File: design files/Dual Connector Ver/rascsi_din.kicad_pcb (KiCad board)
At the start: 2 copper layers, 67.5 x 66.5 mm, 24 parts, among them J1 Raspberry_Pi_2_3, J2 DB25_Female, J3 Conn_02x25_Odd_Even, U1 SN74LS641-1C, U2 SN74LS641-1C, U3 SN74LS641-1C, U4 SN74LS641-1C

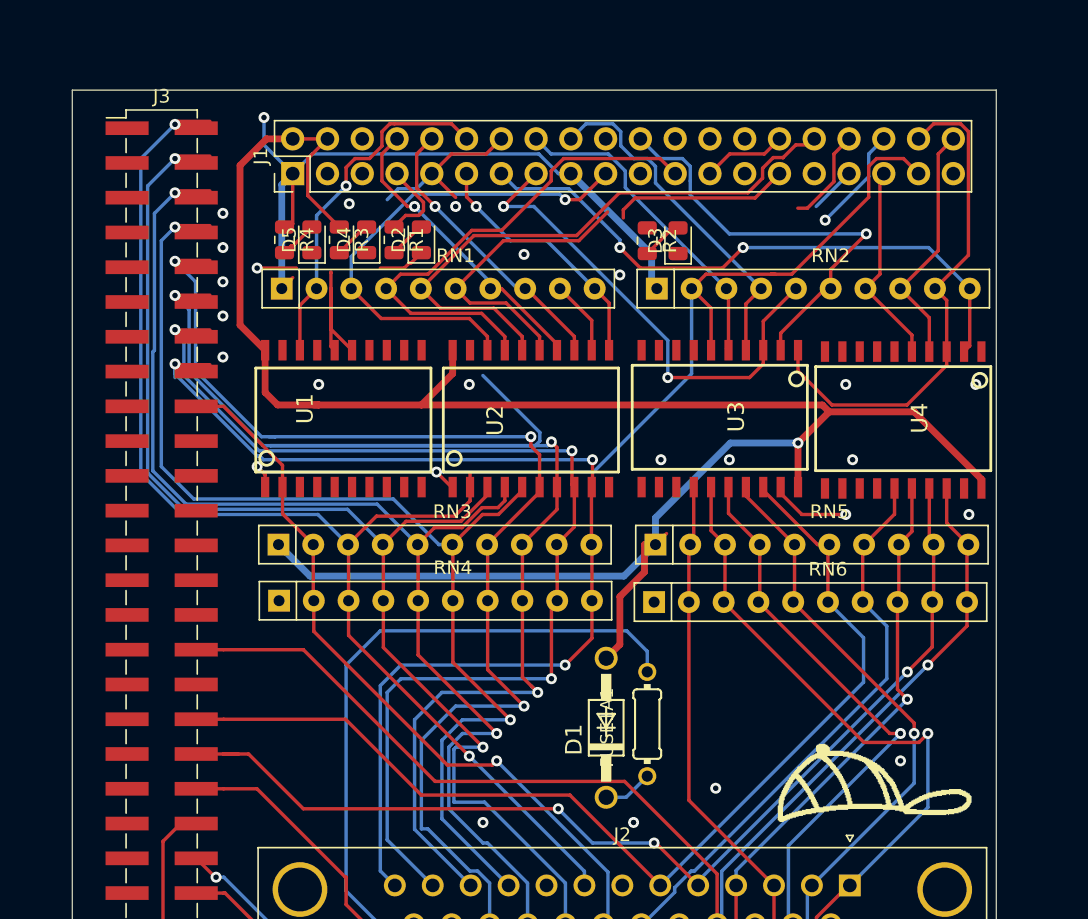
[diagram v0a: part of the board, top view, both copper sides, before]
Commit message: Add silk screen art and clean up labels
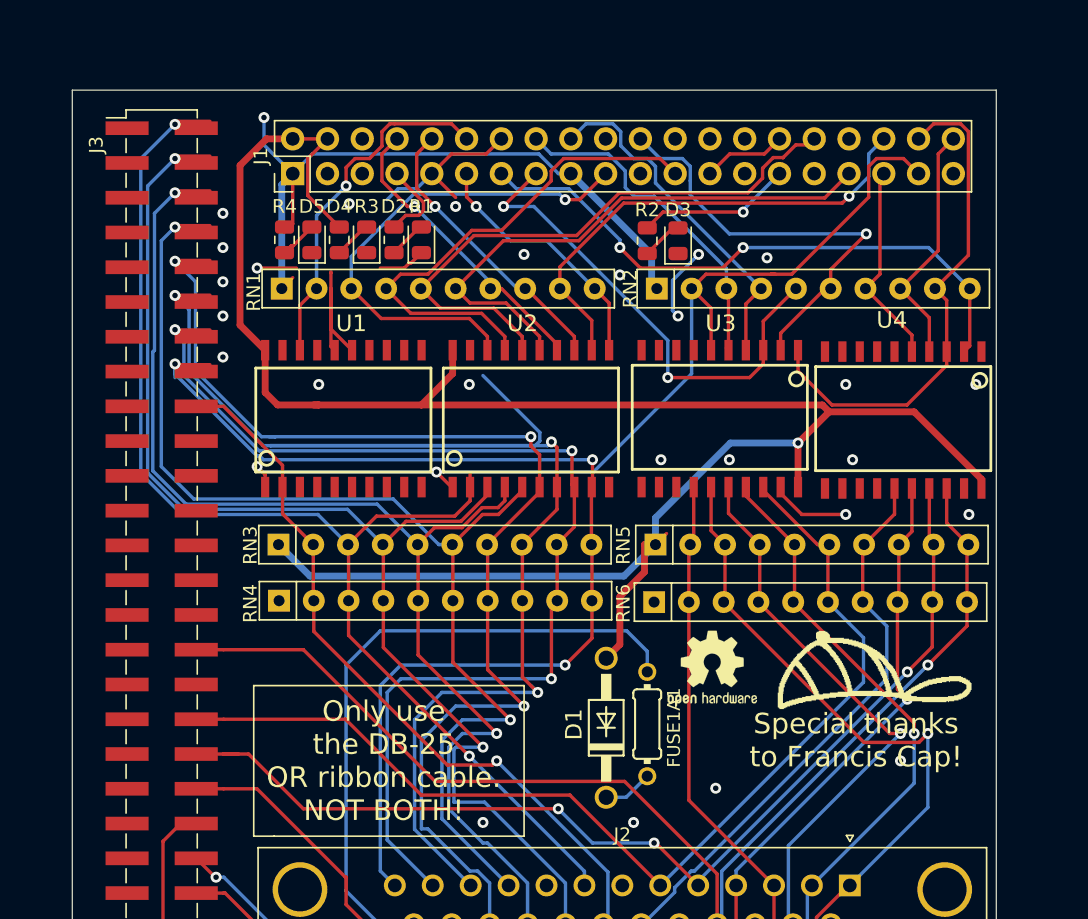
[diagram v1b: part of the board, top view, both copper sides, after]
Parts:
- added REF**: OSHW-Logo2_7.3x6mm_SilkScreen, Symbol:OSHW-Logo2_7.3x6mm_SilkScreen, F.Cu at (100.8, 90.2)
- moved U$1 8.25 mm to (105.5, 93.2)
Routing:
- net PI-D6: track 13.2 -> 35.6 mm
- net PI-D3: track 25.4 -> 40.8 mm
- net DBG_LED: track 13.1 -> 11.2 mm, vias 0 -> 1
- net GND: track 51.5 -> 50.5 mm, vias 24 -> 27
- net PI-REQ: track 23.9 -> 24.8 mm
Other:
- board text added: "Only use the DB-25 OR ribbon cable. NOT BOTH!"
- board text added: "Special thanks to Francis Cap!"

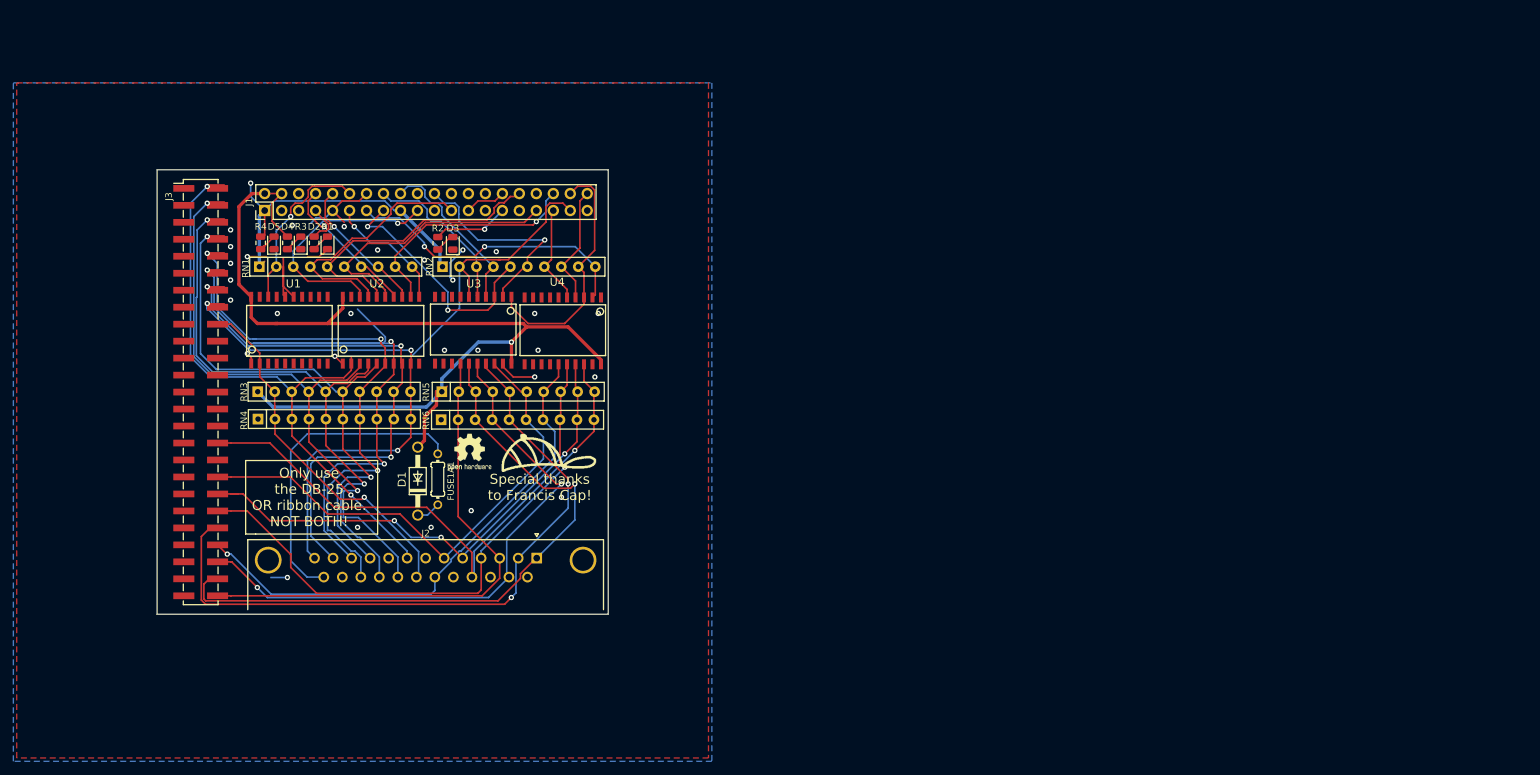
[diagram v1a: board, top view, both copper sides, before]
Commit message: Corrected pinout to match original RaSCSI design.
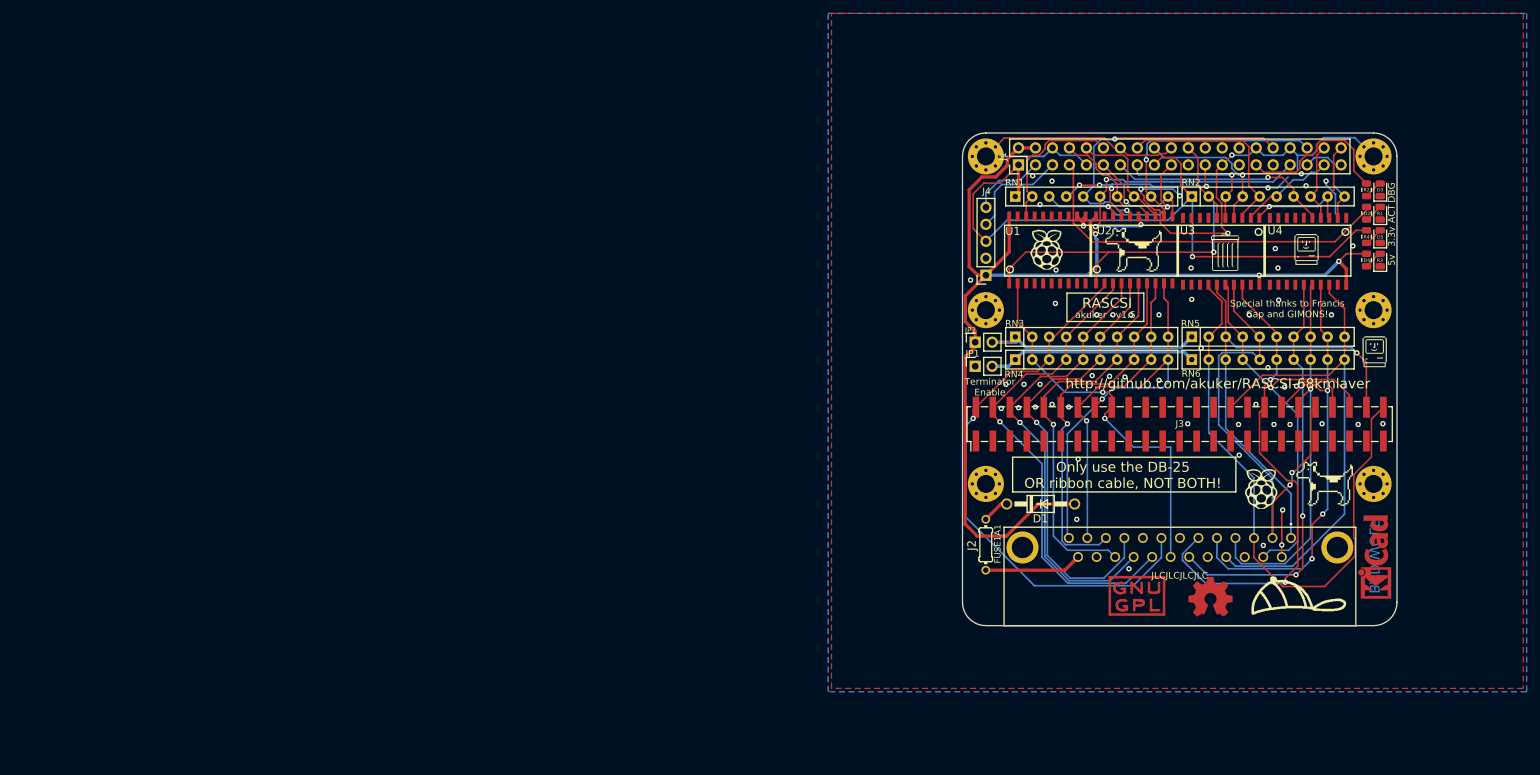
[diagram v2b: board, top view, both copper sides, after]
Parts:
- removed the REF** at (100.8, 90.2)
- added H1: Hole1, MountingHole:MountingHole_2.7mm_M2.5_Pad_Via, F.Cu at (178.0, 46.0)
- added H2: Hole2, MountingHole:MountingHole_2.7mm_M2.5_Pad_Via, F.Cu at (236.0, 46.0)
- added H3: Hole3, MountingHole:MountingHole_2.7mm_M2.5_Pad_Via, F.Cu at (178.0, 69.0)
- added H4: Hole5, MountingHole:MountingHole_2.7mm_M2.5_Pad_Via, F.Cu at (236.0, 69.0)
- added H5: Hole4, MountingHole:MountingHole_2.7mm_M2.5_Pad_Via, F.Cu at (178.0, 95.0)
- added H6: Hole6, MountingHole:MountingHole_2.7mm_M2.5_Pad_Via, F.Cu at (236.0, 95.0)
- added J4: I2C Pinout, Connector_PinSocket_2.54mm:PinSocket_1x05_P2.54mm_Vertical, F.Cu at (178.0, 63.8)
- added JP1: Term_Enable_GND, Connector_PinSocket_2.54mm:PinSocket_1x02_P2.54mm_Vertical, F.Cu at (176.4, 77.4)
- added JP2: Term_Enable_5v, Connector_PinSocket_2.54mm:PinSocket_1x02_P2.54mm_Vertical, F.Cu at (176.4, 73.8)
- added L1: Mac, rascsi_din:mac_happy_small, F.Cu at (226.0, 59.9)
- added L2: Dogcow, rascsi_din:dogcow, F.Cu at (228.7, 95.0)
- added L3: Mac2, rascsi_din:mac_happy_small, F.Cu at (236.2, 75.2)
- added L4: Dogcow2, rascsi_din:dogcow, F.Cu at (200.1, 60.0)
- added L5: Raspberry Pi, rascsi_din:pi_logo, F.Cu at (219.2, 95.8)
- added L6: Mac Trashcan, rascsi_din:mac_trashcan, F.Cu at (213.8, 60.5)
- added L7: Raspberry Pi, rascsi_din:pi_logo, F.Cu at (187.1, 60.0)
- added REF**: KiCad-Logo_5mm_Copper, Symbol:KiCad-Logo_5mm_Copper, F.Cu at (236.7, 105.9)
- added REF**: OSHW-Symbol_6.7x6mm_Copper, Symbol:OSHW-Symbol_6.7x6mm_Copper, F.Cu at (211.6, 111.9)
- added REF**: Symbol_GNU-GPL_CopperTop_Small, Symbol:Symbol_GNU-GPL_CopperTop_Small, F.Cu at (200.6, 112.0)
- J2: value DB25_Female -> DLS3XS6AK44X; footprint Connector_Dsub:DSUB-25_Female_Horizontal_P2.77x2.84mm_EdgePinOffset4.94mm_Housed_MountingHolesOffset7.48mm -> Library_Loader:DLS3XS6AK44X
- R1, R2, R4: value 10k -> 44
- R3: value 10k -> 112
- moved D5 165.5 mm to (237.0, 58.0)
- moved R4 165.5 mm to (234.9, 58.0)
- moved D4 161.5 mm to (237.0, 61.5)
- moved R3 161.5 mm to (234.9, 61.5)
- moved D2 157.6 mm to (237.0, 54.5)
- moved R1 157.5 mm to (234.9, 54.5)
- moved J3 146.5 mm to (207.0, 86.1), turned to 90 degrees
- moved R2 139.2 mm to (234.9, 51.0)
- moved D3 139.0 mm to (237.0, 51.0)
- moved U$1 114.2 mm to (217.7, 114.6)
- moved U1 114.0 mm to (187.2, 60.0)
- moved RN4 113.6 mm to (182.4, 76.4)
- moved RN3 113.6 mm to (182.4, 73.0)
- moved RN1 113.6 mm to (182.4, 52.0)
- moved U2 113.3 mm to (200.2, 60.0)
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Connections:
- J1 pad 13: PI-ATN -> PI-SEL
- J1 pad 15: PI-MSG -> PI-REQ
- J1 pad 16: PI-REQ -> PI-MSG
- J1 pad 22: PI-BSY -> PI-I_O
- J1 pad 3: Net-(J1-Pad3) -> PI_SDA
- J1 pad 35: PI-SEL -> PI-ATN
- J1 pad 37: PI-I_O -> PI-BSY
- J1 pad 38: PI-ACK -> PI-RST
- J1 pad 40: PI-RST -> PI-ACK
- J1 pad 5: Net-(J1-Pad5) -> PI_SCL
- RN3 pad 1: +5V -> Net-(JP2-Pad2)
- RN4 pad 1: GND -> Net-(JP1-Pad2)
- RN5 pad 1: +5V -> Net-(JP2-Pad2)
- RN6 pad 1: GND -> Net-(JP1-Pad2)
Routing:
- net GND: track 50.5 -> 131.8 mm, vias 27 -> 57
- net C-D5: track 108.1 -> 55.1 mm, vias 3 -> 1
- net ACT: track 6.16 -> 56.4 mm
- net +3V3: track 52.4 -> 102.1 mm
- net C-D6: track 82.1 -> 45.7 mm, vias 3 -> 1
- net Net-(JP2-Pad2): track 0.00 -> 35.2 mm
- net TERMPOW: track 47.6 -> 14.6 mm
- net Net-(JP1-Pad2): track 0.00 -> 31.2 mm
- net PI-ATN: track 44.3 -> 14.0 mm, vias 2 -> 0
- net C-MSG: track 103.2 -> 73.6 mm
- net C-RST: track 85.6 -> 57.6 mm
- net C-REQ: track 99.3 -> 71.8 mm
- net C-D4: track 85.5 -> 58.0 mm, vias 3 -> 1
- net C-D7: track 82.4 -> 56.9 mm, vias 3 -> 1
- net C-C_D: track 88.4 -> 64.1 mm, vias 2 -> 1
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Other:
- board size 67.5 x 66.5 mm -> 65 x 73.7 mm
- board text added: "3.3v"
- board text added: "5v"
- board text added: "ACT"
- board text added: "BAD WOLF"
- board text added: "DBG"
- board text added: "JLCJLCJLCJLC"
- board text added: "Only use the DB-25 OR ribbon cable, NOT BOTH!"
- board text added: "RASCSI"
- board text added: "Special thanks to Francis Cap and GIMONS!"
- board text added: "Terminator Enable"
- board text added: "akuker - v1.5"
- board text added: "http://github.com/akuker/RASCSI-68kmlaver"
- board text removed: "Only use the DB-25 OR ribbon cable. NOT BOTH!"
- board text removed: "Special thanks to Francis Cap!"

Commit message: Corrected ACT signal line
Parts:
- removed REF**: KiCad-Logo_5mm_Copper, Symbol:KiCad-Logo_5mm_Copper
- removed REF**: OSHW-Symbol_6.7x6mm_Copper, Symbol:OSHW-Symbol_6.7x6mm_Copper
- removed REF**: Symbol_GNU-GPL_CopperTop_Small, Symbol:Symbol_GNU-GPL_CopperTop_Small
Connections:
- J1 pad 7: ACT -> PI-ACT
- R1 pad 1: ACT -> PI-ACT
- U3 pad 1: PI-ACK -> PI-ACT
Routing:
- net PI-ACT: track 0.00 -> 60.4 mm
- net ACT: track 56.4 -> 0.00 mm
- net PI-ACK: track 23.1 -> 11.4 mm, vias 1 -> 0
- net GND: vias 57 -> 58
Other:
- board text added: "akuker - v1.6"
- board text removed: "akuker - v1.5"
